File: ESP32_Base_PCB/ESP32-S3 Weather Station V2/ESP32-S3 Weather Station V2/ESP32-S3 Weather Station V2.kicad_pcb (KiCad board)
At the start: 2 copper layers, 120 x 60 mm, 40 parts, among them J1 USB_C_Receptacle_USB2.0_16P, J10 A3 of ADC, J11 External Power, J2 Rain Guage, J3 GPIO, J4 Wind Speed/DIR, J5 BME680, J6 Light Density, J7 Soil Mouisture, J8 I2C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

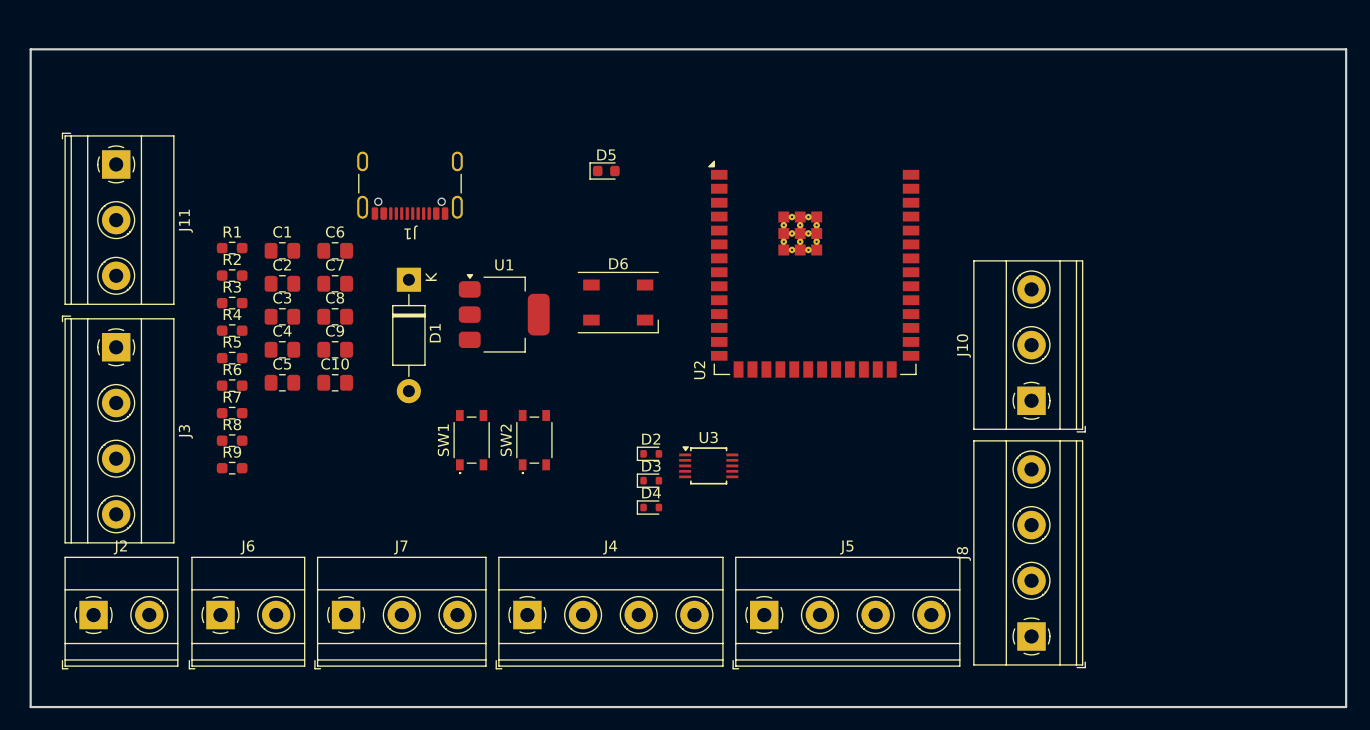
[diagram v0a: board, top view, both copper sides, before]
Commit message: Created GRBR File
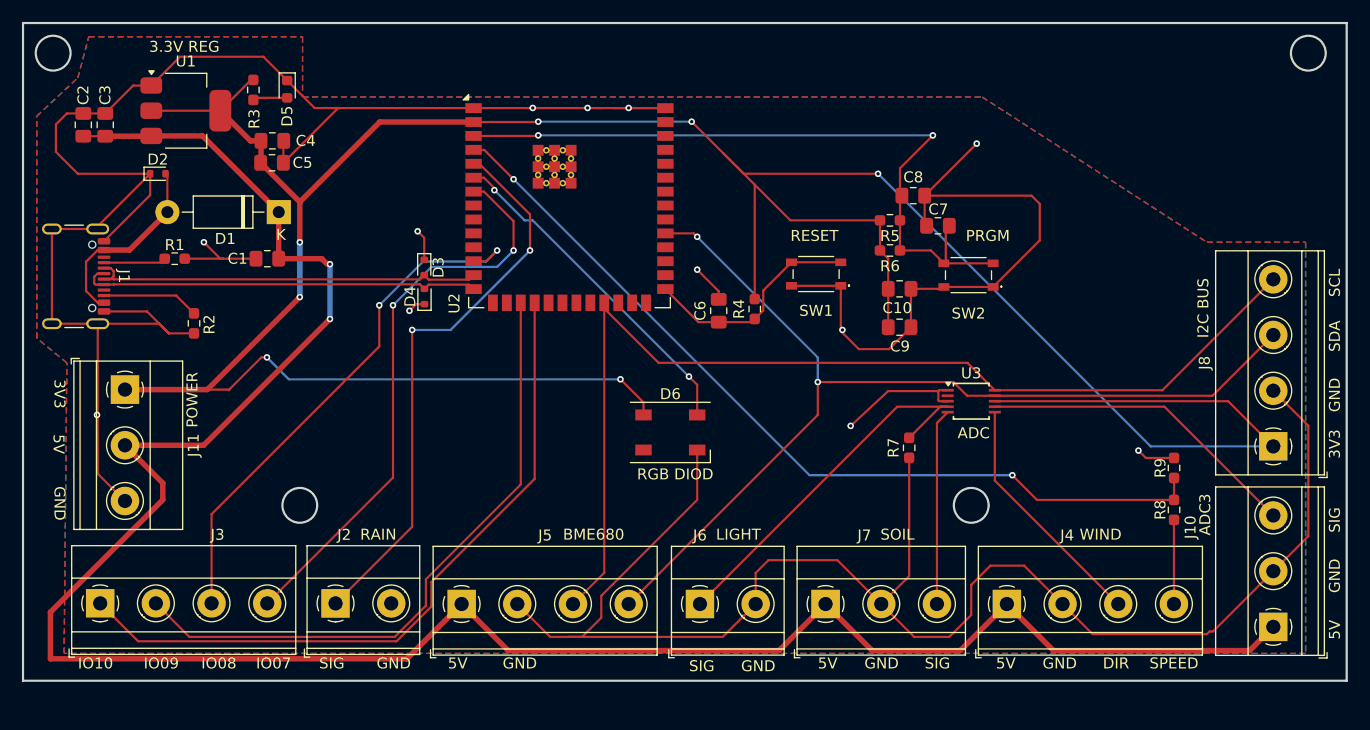
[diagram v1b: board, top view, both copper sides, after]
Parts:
- moved R8 86.1 mm to (205.0, 94.4), turned to -90 degrees
- moved R9 85.9 mm to (205.0, 90.6), turned to -90 degrees
- moved R7 61.8 mm to (180.8, 88.8), turned to 90 degrees
- moved R5 61.3 mm to (179.1, 68.0), turned to 180 degrees
- moved R6 61.3 mm to (179.1, 70.8), turned to 180 degrees
- moved C7 55.2 mm to (183.5, 68.5), turned to 180 degrees
- moved C8 53.9 mm to (181.2, 65.8)
- moved C10 52.2 mm to (180.0, 74.2), turned to 180 degrees
- moved D2 51.8 mm to (112.3, 63.8)
- moved C9 51.5 mm to (180.0, 77.8), turned to 180 degrees
- moved R4 47.7 mm to (166.8, 76.1), turned to 90 degrees
- moved J4 43.8 mm to (189.8, 103.0)
- moved J7 43.8 mm to (173.2, 103.0)
- moved J6 43.8 mm to (161.8, 103.0)
- moved SW2 42.4 mm to (186.2, 73.0), turned to 180 degrees
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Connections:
- J5 pad 3: SDA -> SCL
- J5 pad 4: SCL -> SDA
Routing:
- net GND: track 0.00 -> 385.0 mm, vias 0 -> 12
- net VCC_3V3: track 0.00 -> 262.8 mm, vias 0 -> 7
- net VCC_5V: track 0.00 -> 206.8 mm, vias 0 -> 2
- net SCL: track 0.00 -> 97.5 mm
- net SDA: track 0.00 -> 92.6 mm, vias 0 -> 2
- net SPEED: track 0.00 -> 79.1 mm, vias 0 -> 2
- net CHIP_PU: track 0.00 -> 66.4 mm, vias 0 -> 2
- net GPIO10: track 0.00 -> 64.6 mm
- net GPIO9: track 0.00 -> 58.3 mm
- net GPIO7: track 0.00 -> 52.5 mm, vias 0 -> 2
- net RAIN: track 0.00 -> 51.9 mm, vias 0 -> 2
- net GPIO8: track 0.00 -> 48.9 mm, vias 0 -> 2
- net D+: track 0.00 -> 37.2 mm
- net D-: track 0.00 -> 36.8 mm
- net A0: track 0.00 -> 34.7 mm
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- added copper zone on B.Cu, net GND
- added copper zone on F.Cu, net GND
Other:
- board size 120 x 60 mm -> 120.8 x 60 mm
- board text added: "3.3V REG"
- board text added: "3V3"
- board text added: "5V"
- board text added: "ADC"
- board text added: "ADC3"
- board text added: "BME680"
- board text added: "DIR"
- board text added: "GND"
- board text added: "I2C BUS"
- board text added: "IO07"
- board text added: "IO08"
- board text added: "IO09"
- board text added: "IO10"
- board text added: "LIGHT"
- board text added: "POWER"
- board text added: "PRGM"
- board text added: "RAIN"
- board text added: "RESET"
- board text added: "RGB DIOD"
- board text added: "SCL"
- board text added: "SDA"
- board text added: "SIG"
- board text added: "SOIL"
- board text added: "SPEED"
- board text added: "WIND"
